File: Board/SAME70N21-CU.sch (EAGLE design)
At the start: 35 parts, among them U1 ATSAME70N21A-ANTQFP100_14X14M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

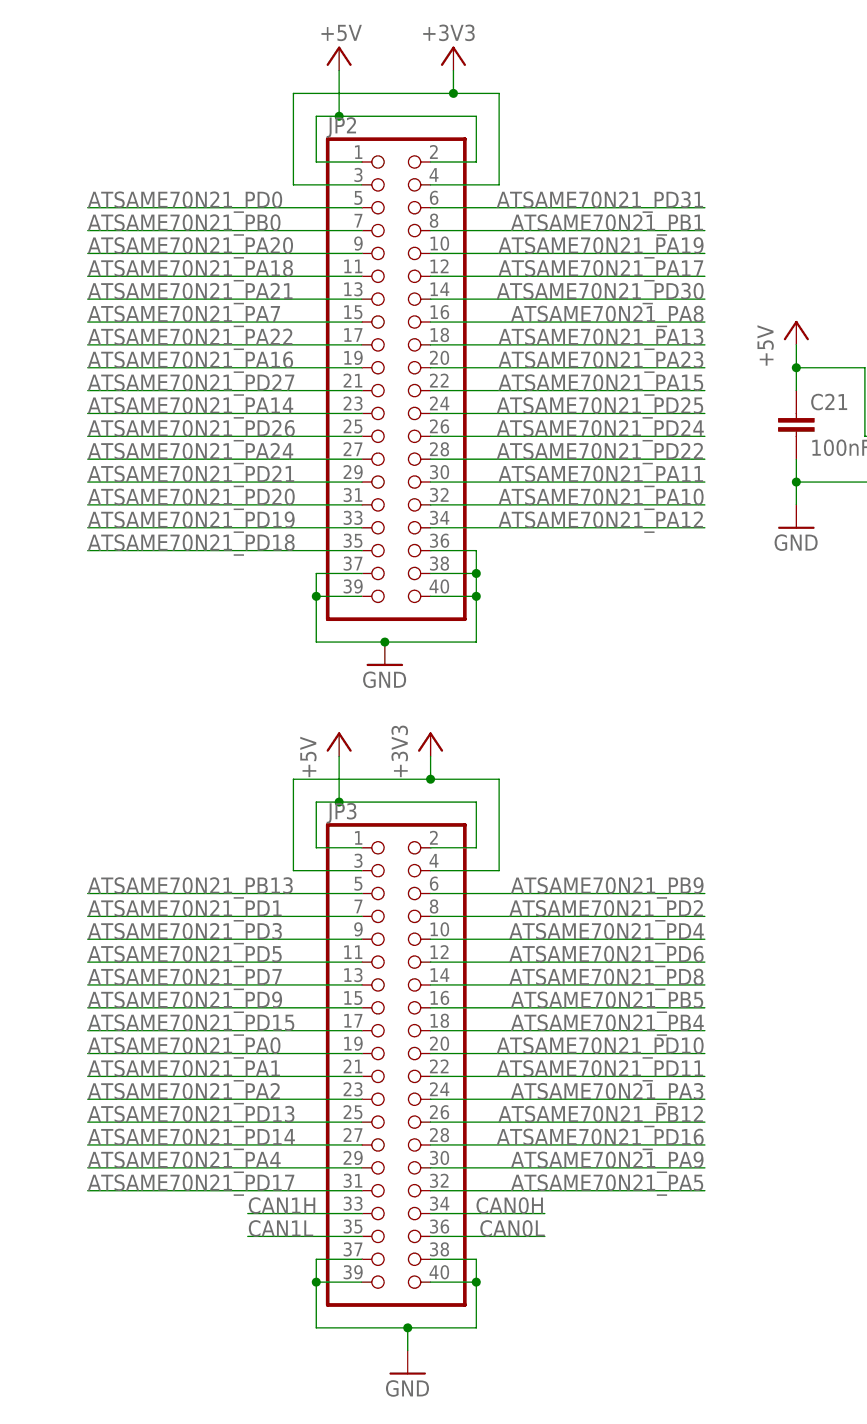
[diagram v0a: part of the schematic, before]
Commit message: Major revision to first board pcb
- reduced board size
- fixed airwires
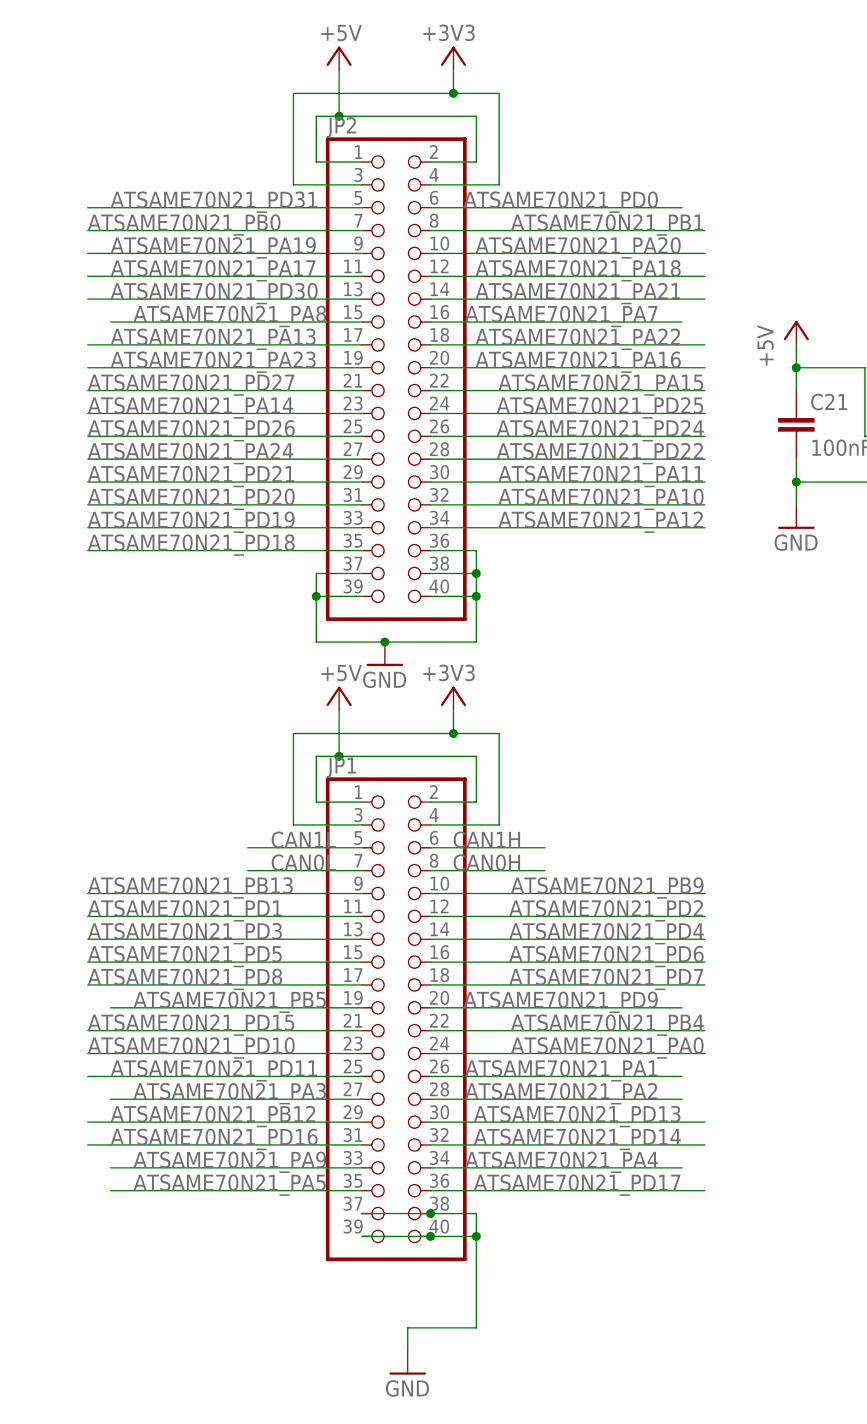
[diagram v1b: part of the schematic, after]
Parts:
- removed JP3: (no value), pinhead:PINHD-2X20
- added JP1: (no value), pinhead:PINHD-2X20
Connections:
- net +3V3: now also JP1.3, JP1.4; no longer JP3.3, JP3.4
- net +5V: now also JP1.1, JP1.2; no longer JP3.1, JP3.2
- net ATSAME70N21_PA0: now also JP1.24; no longer JP3.19
- net ATSAME70N21_PA1: now also JP1.26; no longer JP3.21
- net ATSAME70N21_PA13: now also JP2.17; no longer JP2.18
- net ATSAME70N21_PA16: now also JP2.20; no longer JP2.19
- net ATSAME70N21_PA17: now also JP2.11; no longer JP2.12
- net ATSAME70N21_PA18: now also JP2.12; no longer JP2.11
- net ATSAME70N21_PA19: now also JP2.9; no longer JP2.10
- net ATSAME70N21_PA2: now also JP1.28; no longer JP3.23
- net ATSAME70N21_PA20: now also JP2.10; no longer JP2.9
- net ATSAME70N21_PA21: now also JP2.14; no longer JP2.13
- net ATSAME70N21_PA22: now also JP2.18; no longer JP2.17
- net ATSAME70N21_PA23: now also JP2.19; no longer JP2.20
- net ATSAME70N21_PA3: now also JP1.27; no longer JP3.24
- net ATSAME70N21_PA4: now also JP1.34; no longer JP3.29
- net ATSAME70N21_PA5: now also JP1.35; no longer JP3.32
- net ATSAME70N21_PA7: now also JP2.16; no longer JP2.15
- net ATSAME70N21_PA8: now also JP2.15; no longer JP2.16
- net ATSAME70N21_PA9: now also JP1.33; no longer JP3.30
- net ATSAME70N21_PB12: now also JP1.29; no longer JP3.26
- net ATSAME70N21_PB13: now also JP1.9; no longer JP3.5
- net ATSAME70N21_PB4: now also JP1.22; no longer JP3.18
- net ATSAME70N21_PB5: now also JP1.19; no longer JP3.16
- net ATSAME70N21_PB9: now also JP1.10; no longer JP3.6
- net ATSAME70N21_PD0: now also JP2.6; no longer JP2.5
- net ATSAME70N21_PD1: now also JP1.11; no longer JP3.7
- net ATSAME70N21_PD10: now also JP1.23; no longer JP3.20
- net ATSAME70N21_PD11: now also JP1.25; no longer JP3.22
- net ATSAME70N21_PD13: now also JP1.30; no longer JP3.25
- net ATSAME70N21_PD14: now also JP1.32; no longer JP3.27
- net ATSAME70N21_PD15: now also JP1.21; no longer JP3.17
- net ATSAME70N21_PD16: now also JP1.31; no longer JP3.28
- net ATSAME70N21_PD17: now also JP1.36; no longer JP3.31
- net ATSAME70N21_PD2: now also JP1.12; no longer JP3.8
- net ATSAME70N21_PD3: now also JP1.13; no longer JP3.9
- net ATSAME70N21_PD30: now also JP2.13; no longer JP2.14
- net ATSAME70N21_PD31: now also JP2.5; no longer JP2.6
- net ATSAME70N21_PD4: now also JP1.14; no longer JP3.10
- net ATSAME70N21_PD5: now also JP1.15; no longer JP3.11
- net ATSAME70N21_PD6: now also JP1.16; no longer JP3.12
- net ATSAME70N21_PD7: now also JP1.18; no longer JP3.13
- net ATSAME70N21_PD8: now also JP1.17; no longer JP3.14
- net ATSAME70N21_PD9: now also JP1.20; no longer JP3.15
- net CAN0H: now also JP1.8; no longer JP3.34
- net CAN0L: now also JP1.7; no longer JP3.36
- net CAN1H: now also JP1.6; no longer JP3.33
- net CAN1L: now also JP1.5; no longer JP3.35
- net GND: now also JP1.37, JP1.38, JP1.39, JP1.40; no longer JP3.37, JP3.38, JP3.39, JP3.40
